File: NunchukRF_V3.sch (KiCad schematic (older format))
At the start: 43 parts, among them K1 Buttons, P1 V+, P2 V-, P3 D-, P4 Vbat-, P5 Vbat+, P6 D+, Q1 MOSFET_N, Q2 MOSFET_P, U1 STM32F100C6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

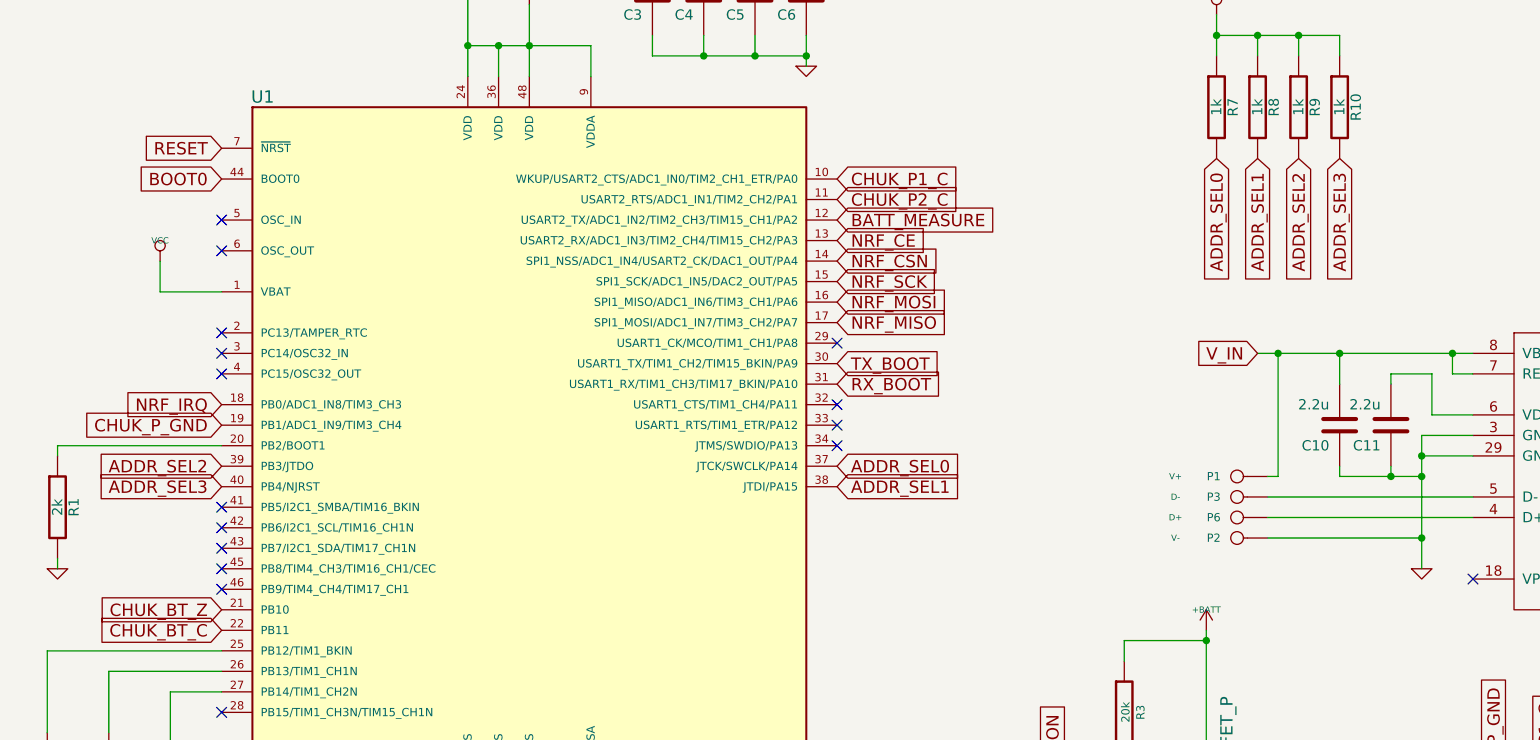
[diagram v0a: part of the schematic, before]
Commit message: Added cp2102 power detect connection to mcu
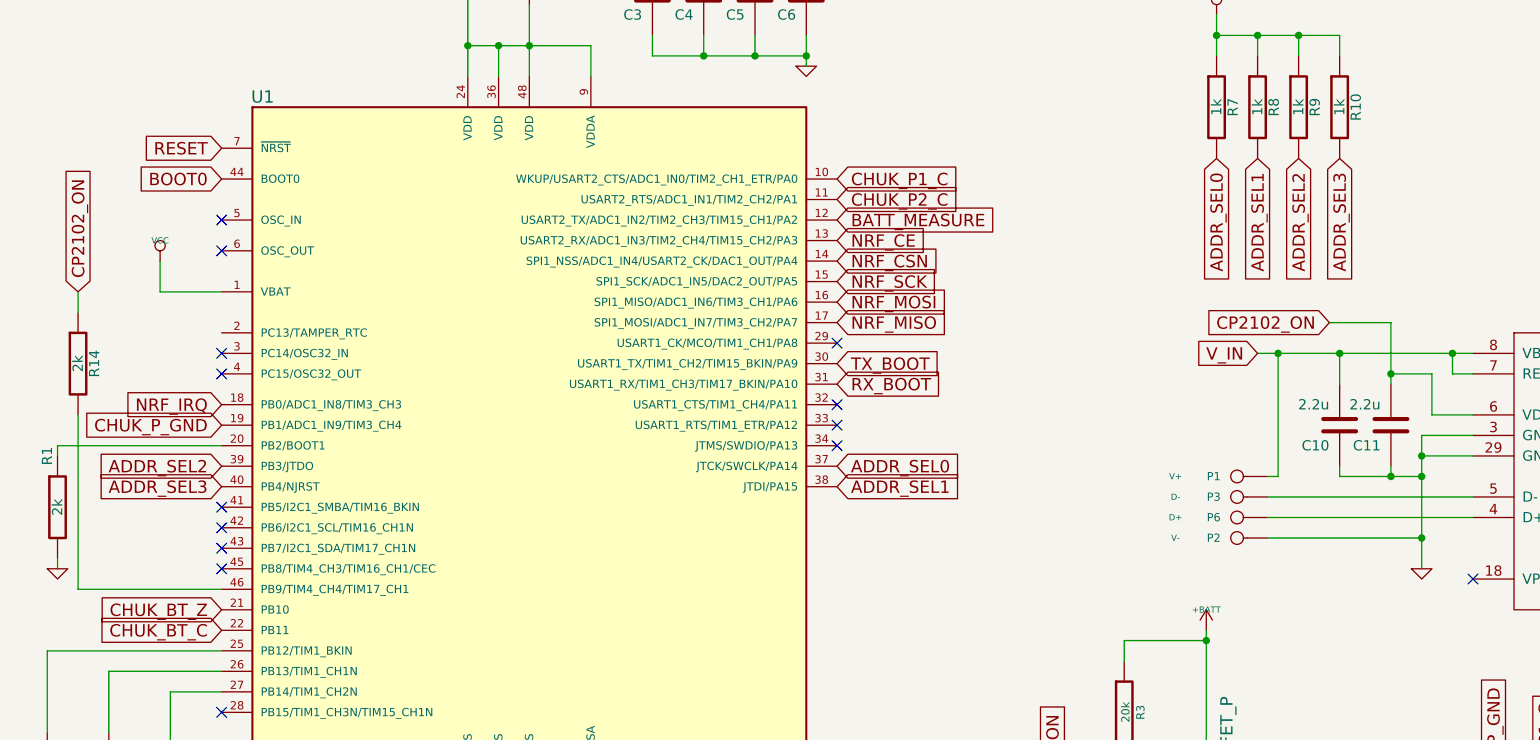
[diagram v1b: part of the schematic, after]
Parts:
- added R14: 2k, Resistors_SMD:R_0603_HandSoldering, symbol R
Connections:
- net at U1.46 (PB9/TIM4_CH4/TIM17_CH1): now also R14.2
- net CP2102_ON: now reaches C11.2, U5.6 (VDD)
- net CP2102_ON: now also R14.1
- no-connect marks 23 -> 21
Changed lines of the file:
@@
 LIBS:crf_1
 LIBS:NunchukRF_V3-cache
-EELAYER 25 0
+EELAYER 24 0
 EELAYER END
 $Descr A4 11693 8268
@@
 U 1 1 55031F95
 P 850 3550
-F 0 "R1" V 930 3550 50  0000 C CNN
+F 0 "R1" V 800 3800 50  0000 C CNN
 F 1 "2k" V 850 3550 50  0000 C CNN
 F 2 "Resistors_SMD:R_0603_HandSoldering" H 850 3550 60  0001 C CNN
@@
 NoConn ~ 4650 3150
 NoConn ~ 4650 3250
-NoConn ~ 1650 2700
 NoConn ~ 1650 2800
 $Comp
@@
 NoConn ~ 1650 2900
 NoConn ~ 1650 3850
-NoConn ~ 1650 3950
 $Comp
 L LED D2
@@
 	7550 2900 7350 2900
 Wire Wire Line
-	7350 2900 7350 2950
+	7350 2650 7350 2950
 Wire Wire Line
 	7750 2900 7650 2900
@@
 Connection ~ 5100 7050
 Connection ~ 5100 6450
+Text GLabel 7050 2650 0    60   Input ~ 0
+CP2102_ON
+Wire Wire Line
+	7050 2650 7350 2650
+Connection ~ 7350 2900
+Text GLabel 950  2500 1    60   Input ~ 0
+CP2102_ON
+$Comp
+L R R14
+U 1 1 55D51D5B
+P 950 2850
+F 0 "R14" V 1030 2850 50  0000 C CNN
+F 1 "2k" V 950 2850 50  0000 C CNN
+F 2 "Resistors_SMD:R_0603_HandSoldering" H 950 2850 60  0001 C CNN
+F 3 "" H 950 2850 60  0001 C CNN
+	1    950  2850
+	1    0    0    -1
+$EndComp
+Wire Wire Line
+	950  2600 950  2500
+Wire Wire Line
+	950  3100 950  3950
+Wire Wire Line
+	950  3950 1650 3950
 $EndSCHEMATC

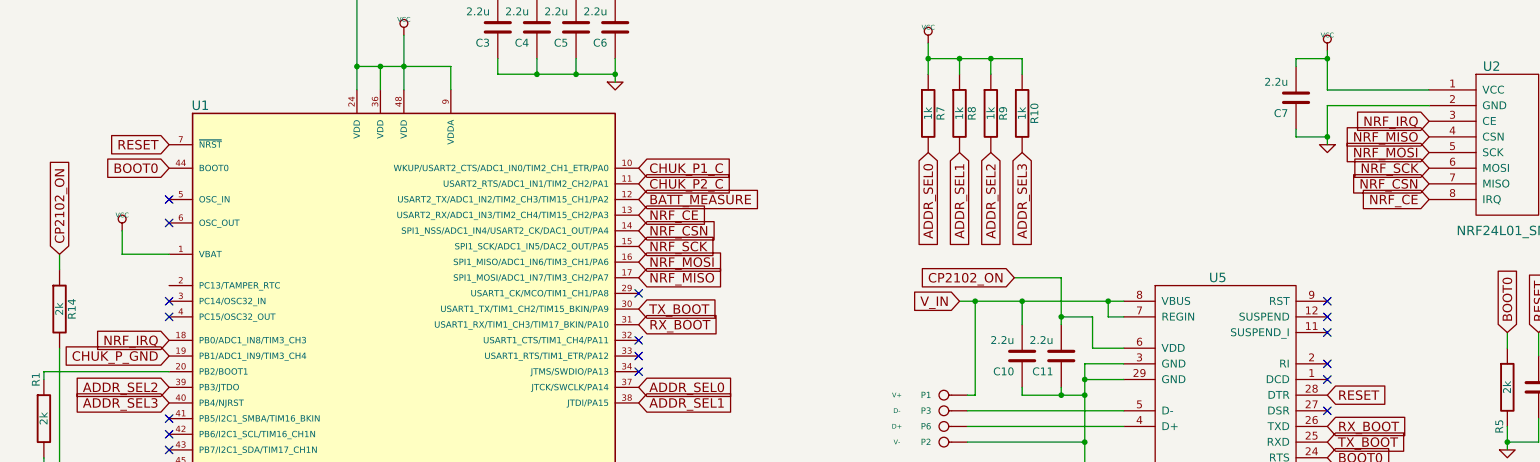
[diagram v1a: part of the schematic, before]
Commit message: Updated NRF labels
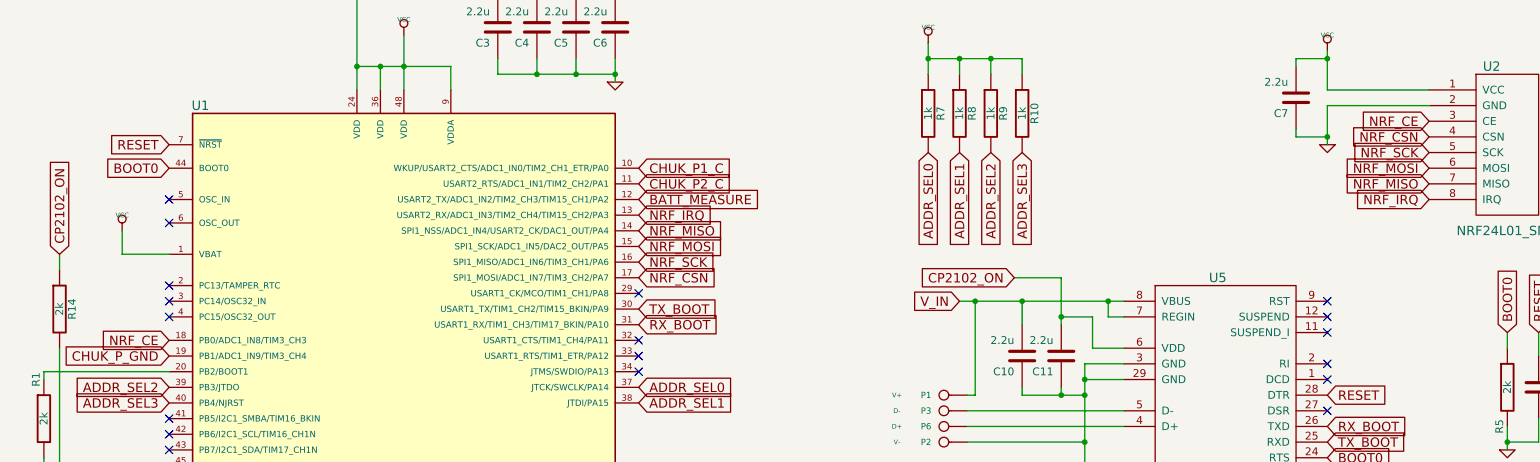
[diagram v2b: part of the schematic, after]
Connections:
- net NRF_CE: now also U1.18 (PB0/ADC1_IN8/TIM3_CH3), U2.3 (CE); no longer U1.13 (USART2_RX/ADC1_IN3/TIM2_CH4/TIM15_CH2/PA3), U2.8 (IRQ)
- net NRF_CSN: now also U1.17 (SPI1_MOSI/ADC1_IN7/TIM3_CH2/PA7), U2.4 (CSN); no longer U1.14 (SPI1_NSS/ADC1_IN4/USART2_CK/DAC1_OUT/PA4), U2.7 (MISO)
- net NRF_IRQ: now also U1.13 (USART2_RX/ADC1_IN3/TIM2_CH4/TIM15_CH2/PA3), U2.8 (IRQ); no longer U1.18 (PB0/ADC1_IN8/TIM3_CH3), U2.3 (CE)
- net NRF_MISO: now also U1.14 (SPI1_NSS/ADC1_IN4/USART2_CK/DAC1_OUT/PA4), U2.7 (MISO); no longer U1.17 (SPI1_MOSI/ADC1_IN7/TIM3_CH2/PA7), U2.4 (CSN)
- net NRF_MOSI: now also U1.15 (SPI1_SCK/ADC1_IN5/DAC2_OUT/PA5), U2.6 (MOSI); no longer U1.16 (SPI1_MISO/ADC1_IN6/TIM3_CH1/PA6), U2.5 (SCK)
- net NRF_SCK: now also U1.16 (SPI1_MISO/ADC1_IN6/TIM3_CH1/PA6), U2.5 (SCK); no longer U1.15 (SPI1_SCK/ADC1_IN5/DAC2_OUT/PA5), U2.6 (MOSI)
- no-connect marks 21 -> 22
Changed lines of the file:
@@
 	-1   0    0    -1
 $EndComp
+Text GLabel 9700 1650 0    60   Input ~ 0
+NRF_CE
+Text GLabel 9700 1750 0    60   Input ~ 0
+NRF_CSN
+Text GLabel 9700 1850 0    60   Input ~ 0
+NRF_SCK
+Text GLabel 9700 1950 0    60   Input ~ 0
+NRF_MOSI
+Text GLabel 9700 2050 0    60   Input ~ 0
+NRF_MISO
 Text GLabel 9700 2150 0    60   Input ~ 0
+NRF_IRQ
+Wire Wire Line
+	9700 1550 9050 1550
+Wire Wire Line
+	9050 1550 9050 1800
+Wire Wire Line
+	9050 1200 9050 1450
+Wire Wire Line
+	9050 1450 9700 1450
+Text GLabel 1650 3050 0    60   Input ~ 0
 NRF_CE
-Text GLabel 9700 2050 0    60   Input ~ 0
+Text GLabel 4650 2650 2    60   Input ~ 0
 NRF_CSN
-Text GLabel 9700 1950 0    60   Input ~ 0
+Text GLabel 4650 2550 2    60   Input ~ 0
 NRF_SCK
-Text GLabel 9700 1850 0    60   Input ~ 0
+Text GLabel 4650 2450 2    60   Input ~ 0
 NRF_MOSI
-Text GLabel 9700 1750 0    60   Input ~ 0
+Text GLabel 4650 2350 2    60   Input ~ 0
 NRF_MISO
-Text GLabel 9700 1650 0    60   Input ~ 0
-NRF_IRQ
-Wire Wire Line
-	9700 1550 9050 1550
-Wire Wire Line
-	9050 1550 9050 1800
-Wire Wire Line
-	9050 1200 9050 1450
-Wire Wire Line
-	9050 1450 9700 1450
 Text GLabel 4650 2250 2    60   Input ~ 0
-NRF_CE
-Text GLabel 4650 2350 2    60   Input ~ 0
-NRF_CSN
-Text GLabel 4650 2450 2    60   Input ~ 0
-NRF_SCK
-Text GLabel 4650 2550 2    60   Input ~ 0
-NRF_MOSI
-Text GLabel 4650 2650 2    60   Input ~ 0
-NRF_MISO
-Text GLabel 1650 3050 0    60   Input ~ 0
 NRF_IRQ
 $Comp
@@
 Wire Wire Line
 	950  3950 1650 3950
+NoConn ~ 1650 2700
 $EndSCHEMATC

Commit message: Updated 3d pictures and saved using the latest kicad version
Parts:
- C1, C10, C11, C2, C3, C4, C5, C6, C7, C8, C9: symbol C -> C-RESCUE-NunchukRF_V3
- D1, D2, D3: symbol LED -> LED-RESCUE-NunchukRF_V3
- R1, R10, R11, R12, R13, R14, R2, R3, R4, R5, R6, R7, R8, R9: symbol R -> R-RESCUE-NunchukRF_V3
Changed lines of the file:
@@
 EESchema Schematic File Version 2
+LIBS:NunchukRF_V3-rescue
 LIBS:power
 LIBS:device
@@
 LIBS:crf_1
 LIBS:NunchukRF_V3-cache
-EELAYER 24 0
+EELAYER 25 0
 EELAYER END
 $Descr A4 11693 8268
@@
 $EndDescr
 $Comp
-L GND #PWR01
+L GND-RESCUE-NunchukRF_V3 #PWR01
 U 1 1 55031F29
 P 3450 5200
@@
 $EndComp
 $Comp
-L C C3
+L C-RESCUE-NunchukRF_V3 C3
 U 1 1 55031F35
 P 3750 1050
@@
 NoConn ~ 1650 2300
 $Comp
-L R R1
+L R-RESCUE-NunchukRF_V3 R1
 U 1 1 55031F95
 P 850 3550
@@
 $EndComp
 $Comp
-L GND #PWR02
+L GND-RESCUE-NunchukRF_V3 #PWR02
 U 1 1 55031F9C
 P 850 3850
@@
 BOOT0
 $Comp
-L LED D1
+L LED-RESCUE-NunchukRF_V3 D1
 U 1 1 55031FBD
 P 800 4850
@@
 $EndComp
 $Comp
-L R R2
+L R-RESCUE-NunchukRF_V3 R2
 U 1 1 55031FC4
 P 800 5350
@@
 $EndComp
 $Comp
-L GND #PWR03
+L GND-RESCUE-NunchukRF_V3 #PWR03
 U 1 1 55031FCB
 P 800 5650
@@
 NoConn ~ 1650 2800
 $Comp
-L C C8
+L C-RESCUE-NunchukRF_V3 C8
 U 1 1 55031FE9
 P 10400 3350
@@
 BOOT0
 $Comp
-L R R5
+L R-RESCUE-NunchukRF_V3 R5
 U 1 1 5503201C
 P 10200 3350
@@
 $EndComp
 $Comp
-L GND #PWR04
+L GND-RESCUE-NunchukRF_V3 #PWR04
 U 1 1 55032023
 P 10200 3750
@@
 $EndComp
 $Comp
-L GND #PWR05
+L GND-RESCUE-NunchukRF_V3 #PWR05
 U 1 1 550A02B4
 P 9050 1800
@@
 NRF_IRQ
 $Comp
-L GND #PWR06
+L GND-RESCUE-NunchukRF_V3 #PWR06
 U 1 1 55031F3C
 P 4500 1400
@@
 $EndComp
 $Comp
-L C C4
+L C-RESCUE-NunchukRF_V3 C4
 U 1 1 550A1E4F
 P 4000 1050
@@
 $EndComp
 $Comp
-L C C5
+L C-RESCUE-NunchukRF_V3 C5
 U 1 1 550A1E75
 P 4250 1050
@@
 $EndComp
 $Comp
-L C C6
+L C-RESCUE-NunchukRF_V3 C6
 U 1 1 550A1E9C
 P 4500 1050
@@
 CHUK_P_GND
 $Comp
-L C C7
+L C-RESCUE-NunchukRF_V3 C7
 U 1 1 550A6767
 P 8850 1500
@@
 NoConn ~ 1650 3850
 $Comp
-L LED D2
+L LED-RESCUE-NunchukRF_V3 D2
 U 1 1 550C130D
 P 1100 4850
@@
 $EndComp
 $Comp
-L R R6
+L R-RESCUE-NunchukRF_V3 R6
 U 1 1 550C1313
 P 1100 5350
@@
 $EndComp
 $Comp
-L GND #PWR09
+L GND-RESCUE-NunchukRF_V3 #PWR09
 U 1 1 550C1319
 P 1100 5650
@@
 NoConn ~ 1650 4550
 $Comp
-L R R10
+L R-RESCUE-NunchukRF_V3 R10
 U 1 1 550C2D8C
 P 7100 1600
@@
 $EndComp
 $Comp
-L R R9
+L R-RESCUE-NunchukRF_V3 R9
 U 1 1 550C2E7D
 P 6900 1600
@@
 $EndComp
 $Comp
-L R R8
+L R-RESCUE-NunchukRF_V3 R8
 U 1 1 550C2EBB
 P 6700 1600
@@
 $EndComp
 $Comp
-L R R7
+L R-RESCUE-NunchukRF_V3 R7
 U 1 1 550C2F09
 P 6500 1600
@@
 ADDR_SEL3
 $Comp
-L GND #PWR010
+L GND-RESCUE-NunchukRF_V3 #PWR010
 U 1 1 559447F0
 P 3050 7250
@@
 $EndComp
 $Comp
-L R R11
+L R-RESCUE-NunchukRF_V3 R11
 U 1 1 559448C1
 P 2450 6850
@@
 Connection ~ 3050 7150
 $Comp
-L C C1
+L C-RESCUE-NunchukRF_V3 C1
 U 1 1 55951FEA
 P 2900 6750
@@
 $EndComp
 $Comp
-L C C2
+L C-RESCUE-NunchukRF_V3 C2
 U 1 1 55951FF0
 P 5100 6750
@@
 Connection ~ 4850 6450
 $Comp
-L GND #PWR011
+L GND-RESCUE-NunchukRF_V3 #PWR011
 U 1 1 559528D4
 P 5100 7150
@@
 $EndComp
 $Comp
-L LED D3
+L LED-RESCUE-NunchukRF_V3 D3
 U 1 1 5595BA71
 P 1250 6650
@@
 $EndComp
 $Comp
-L R R12
+L R-RESCUE-NunchukRF_V3 R12
 U 1 1 5595BA81
 P 1250 7150
@@
 	1250 6900 1250 6850
 $Comp
-L C C9
+L C-RESCUE-NunchukRF_V3 C9
 U 1 1 5595BF35
 P 850 6850
@@
 Connection ~ 1250 6450
 $Comp
-L GND #PWR012
+L GND-RESCUE-NunchukRF_V3 #PWR012
 U 1 1 5596F1DC
 P 850 7500
@@
 $EndComp
 $Comp
-L GND #PWR013
+L GND-RESCUE-NunchukRF_V3 #PWR013
 U 1 1 55D325C4
 P 10150 5550
@@
 	6750 3700 7500 3700
 $Comp
-L GND #PWR021
+L GND-RESCUE-NunchukRF_V3 #PWR021
 U 1 1 55D37CC3
 P 7500 3850
@@
 Connection ~ 7500 3700
 $Comp
-L C C10
+L C-RESCUE-NunchukRF_V3 C10
 U 1 1 55D3805A
 P 7100 3150
@@
 $EndComp
 $Comp
-L C C11
+L C-RESCUE-NunchukRF_V3 C11
 U 1 1 55D380E8
 P 7350 3150
@@
 NoConn ~ 1650 3550
 $Comp
-L R R13
+L R-RESCUE-NunchukRF_V3 R13
 U 1 1 55D44D04
 P 6450 6050
@@
 $EndComp
 $Comp
-L R R4
+L R-RESCUE-NunchukRF_V3 R4
 U 1 1 55D44D8B
 P 6450 5450
@@
 $EndComp
 $Comp
-L GND #PWR025
+L GND-RESCUE-NunchukRF_V3 #PWR025
 U 1 1 55D45E64
 P 6450 6400
@@
 $EndComp
 $Comp
-L R R3
+L R-RESCUE-NunchukRF_V3 R3
 U 1 1 55D49417
 P 6050 4550
@@
 CP2102_ON
 $Comp
-L R R14
+L R-RESCUE-NunchukRF_V3 R14
 U 1 1 55D51D5B
 P 950 2850

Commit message: Changed CP2102 footprint
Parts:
- U5: footprint w_smd_qfn:qfn-28 -> Housings_DFN_QFN:QFN-28-1EP_5x5mm_Pitch0.5mm
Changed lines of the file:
@@
 F 0 "U5" H 8350 4050 60  0000 C CNN
 F 1 "CP2102" H 8400 2600 60  0000 C CNN
-F 2 "w_smd_qfn:qfn-28" H 8300 3700 60  0001 C CNN
+F 2 "Housings_DFN_QFN:QFN-28-1EP_5x5mm_Pitch0.5mm" H 8300 3700 60  0001 C CNN
 F 3 "" H 8300 3700 60  0000 C CNN
 	1    8400 3350

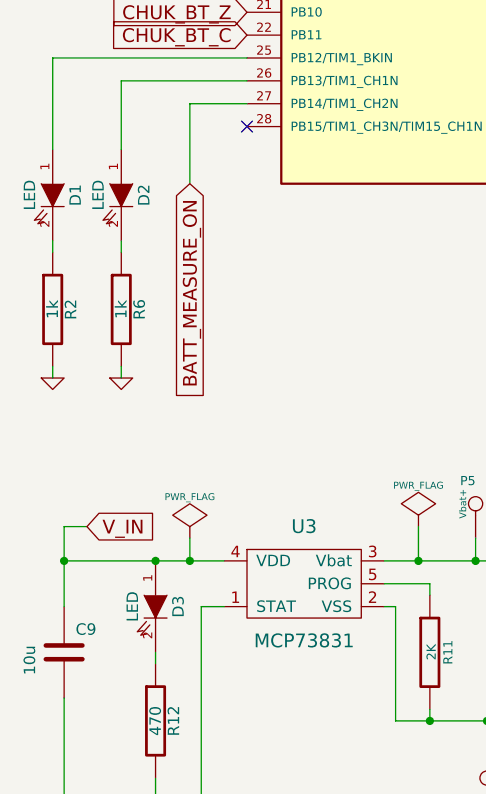
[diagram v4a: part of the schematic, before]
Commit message: Moved nrf, changed button connector, updated labels
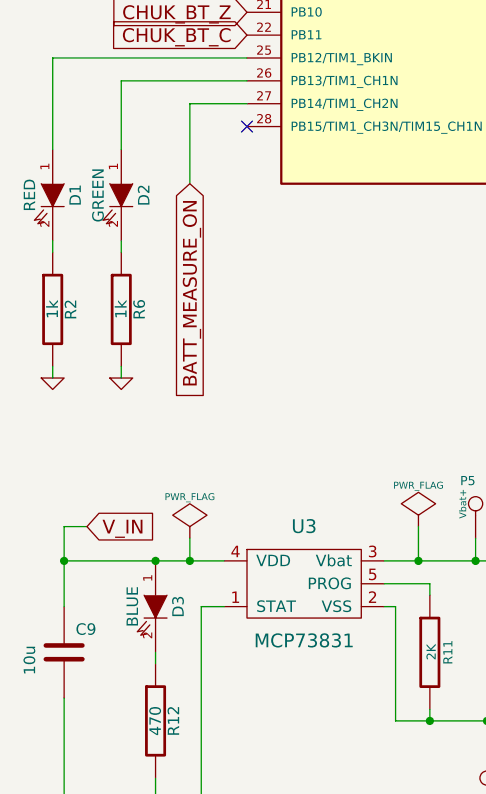
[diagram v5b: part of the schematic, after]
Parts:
- D1: value LED -> RED
- D2: value LED -> GREEN
- D3: value LED -> BLUE
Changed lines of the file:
@@
 P 800 4850
 F 0 "D1" H 800 4950 50  0000 C CNN
-F 1 "LED" H 800 4750 50  0000 C CNN
+F 1 "RED" H 800 4750 50  0000 C CNN
 F 2 "LEDs:LED-0805" H 800 4850 60  0001 C CNN
 F 3 "" H 800 4850 60  0001 C CNN
@@
 P 1100 4850
 F 0 "D2" H 1100 4950 50  0000 C CNN
-F 1 "LED" H 1100 4750 50  0000 C CNN
+F 1 "GREEN" H 1100 4750 50  0000 C CNN
 F 2 "LEDs:LED-0805" H 1100 4850 60  0001 C CNN
 F 3 "" H 1100 4850 60  0001 C CNN
@@
 P 1250 6650
 F 0 "D3" H 1250 6750 50  0000 C CNN
-F 1 "LED" H 1250 6550 50  0000 C CNN
+F 1 "BLUE" H 1250 6550 50  0000 C CNN
 F 2 "LEDs:LED-0805" H 1250 6650 60  0001 C CNN
 F 3 "" H 1250 6650 60  0001 C CNN
